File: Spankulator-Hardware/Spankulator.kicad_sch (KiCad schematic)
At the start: 106 parts, among them J1 3.5mm Jack, J12 Arduino Socket, J13 Arduino Socket, J2 2x5 Header, J3 3.5mm Jack, J4 3.5mm Jack, J5 3.5mm Jack, J6 3.5mm Jack, J7 2x5 Header, J9 Display Header, Q1 2N3904, Q2 VP2106/ZVP3306A, Q3 2N7000, Q4 VP2106/ZVP3306A, Q5 2N7000, Q7 2N7000, Q8 2N7000, SW1 Adj, SW2 Push Button, SW3 Push Button, SW4 Push Button, SW5 Push Button, SW6 Push Button, SW7 Push Button, SW8 Push Button, U1 TL072CP, U2 CD4013BE, U3 TL072CP, U4 MC78L05_TO92, U5 LP2950-3.3_TO92, U6 MAX7480, U7 MB85RC256

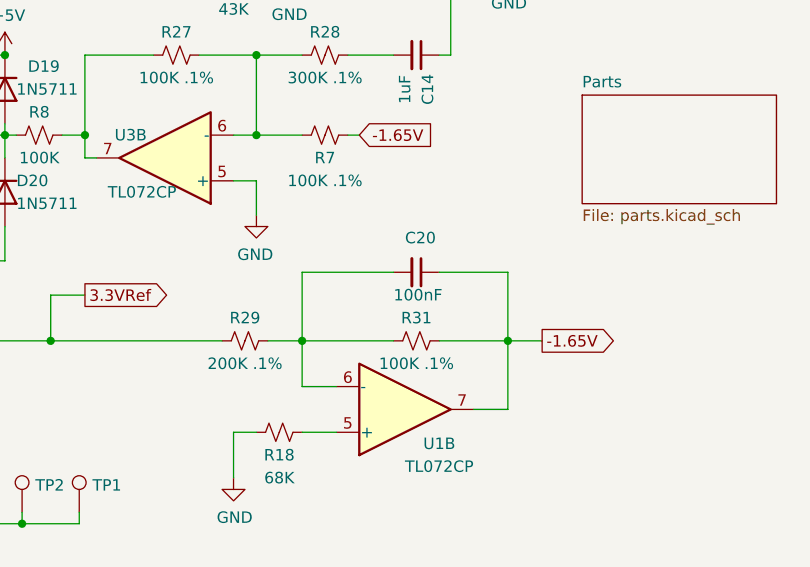
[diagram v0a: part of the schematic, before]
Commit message: Fixes parts too close
Fixes gain pot bumping into Exp connector.
Moves all TPs to board top
More components lay flat now
Adds Argh Ptoo face to silkscreen
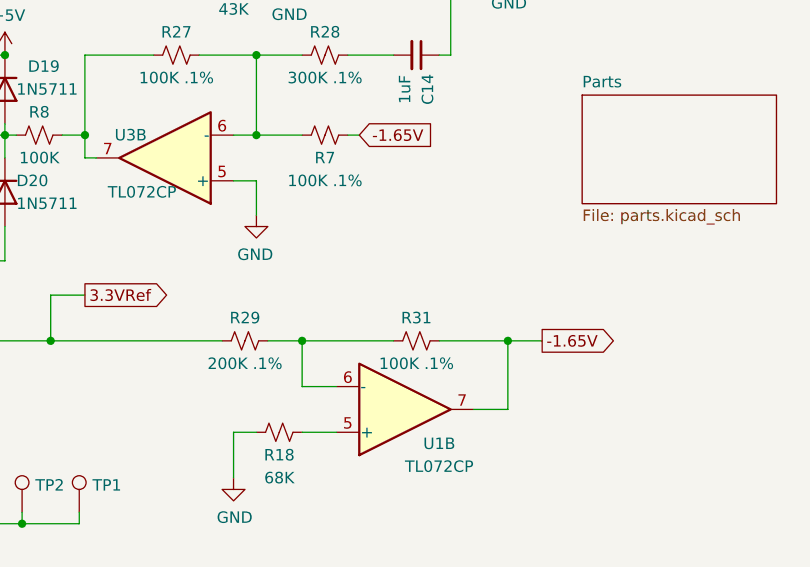
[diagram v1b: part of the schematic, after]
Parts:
- removed C20: 100nF, Capacitor_THT:C_Disc_D4.3mm_W1.9mm_P5.00mm, symbol Device:C_Small
- C16: LCSC Part # (none) -> C263193
- D8: footprint Diode_THT:D_DO-35_SOD27_P2.54mm_Vertical_AnodeUp -> Diode_THT:D_DO-35_SOD27_P7.62mm_Horizontal
- R16, R30, R31: footprint Resistor_THT:R_Axial_DIN0207_L6.3mm_D2.5mm_P2.54mm_Vertical -> Resistor_THT:R_Axial_DIN0207_L6.3mm_D2.5mm_P10.16mm_Horizontal
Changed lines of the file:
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@@
   (title_block
     (title "Spankulator")
-    (rev "5.1")
+    (rev "5.2")
     (company "Greenface Labs")
   )
@@
     (stroke (width 0) (type default) (color 0 0 0 0))
   )
-  (wire (pts (xy 247.65 128.27) (xy 247.65 135.89))
-    (stroke (width 0) (type default) (color 0 0 0 0))
-  )
   (wire (pts (xy 149.86 168.91) (xy 149.86 182.88))
     (stroke (width 0) (type default) (color 0 0 0 0))
@@
     (stroke (width 0) (type default) (color 0 0 0 0))
   )
-  (wire (pts (xy 224.79 128.27) (xy 224.79 135.89))
-    (stroke (width 0) (type default) (color 0 0 0 0))
-  )
   (wire (pts (xy 74.93 91.44) (xy 71.12 91.44))
     (stroke (width 0) (type default) (color 0 0 0 0))
@@
     (stroke (width 0) (type default) (color 0 0 0 0))
   )
-  (wire (pts (xy 240.03 128.27) (xy 247.65 128.27))
-    (stroke (width 0) (type default) (color 0 0 0 0))
-  )
   (wire (pts (xy 160.02 128.27) (xy 160.02 125.73))
     (stroke (width 0) (type default) (color 0 0 0 0))
@@
     (stroke (width 0) (type default) (color 0 0 0 0))
   )
-  (wire (pts (xy 234.95 128.27) (xy 224.79 128.27))
-    (stroke (width 0) (type default) (color 0 0 0 0))
-  )
   (wire (pts (xy 69.85 60.96) (xy 101.6 60.96))
     (stroke (width 0) (type default) (color 0 0 0 0))
@@
     (property "Reference" "R31" (id 0) (at 237.49 133.35 90))
     (property "Value" "100K .1%" (id 1) (at 237.49 138.43 90))
-    (property "Footprint" "Resistor_THT:R_Axial_DIN0207_L6.3mm_D2.5mm_P2.54mm_Vertical" (id 2) (at 237.49 135.89 0)
+    (property "Footprint" "Resistor_THT:R_Axial_DIN0207_L6.3mm_D2.5mm_P10.16mm_Horizontal" (id 2) (at 237.49 135.89 0)
       (effects (font (size 1.27 1.27)) hide)
     )
@@
       (effects (font (size 1.27 1.27)) hide)
     )
+    (property "LCSC Part #" "C263193" (id 5) (at 160.02 123.19 0)
+      (effects (font (size 1.27 1.27)) hide)
+    )
     (pin "1")
     (pin "2")
@@
     (property "Reference" "R30" (id 0) (at 191.77 60.96 90))
     (property "Value" "95.3K 1%" (id 1) (at 191.77 66.04 90))
-    (property "Footprint" "Resistor_THT:R_Axial_DIN0207_L6.3mm_D2.5mm_P2.54mm_Vertical" (id 2) (at 191.77 63.5 0)
+    (property "Footprint" "Resistor_THT:R_Axial_DIN0207_L6.3mm_D2.5mm_P10.16mm_Horizontal" (id 2) (at 191.77 63.5 0)
       (effects (font (size 1.27 1.27)) hide)
     )
@@
     (property "Reference" "R16" (id 0) (at 201.93 17.78 0))
     (property "Value" "100K" (id 1) (at 201.93 20.32 0))
-    (property "Footprint" "Resistor_THT:R_Axial_DIN0207_L6.3mm_D2.5mm_P2.54mm_Vertical" (id 2) (at 198.12 19.05 0)
+    (property "Footprint" "Resistor_THT:R_Axial_DIN0207_L6.3mm_D2.5mm_P10.16mm_Horizontal" (id 2) (at 198.12 19.05 0)
       (effects (font (size 1.27 1.27)) hide)
     )
@@
     (pin "3")
   )
-  (symbol (lib_id "Device:C_Small") (at 237.49 128.27 270) (unit 1)
-    (in_bom yes) (on_board yes)
-    (property "Reference" "C20" (id 0) (at 236.22 124.46 90)
-      (effects (font (size 1.27 1.27)) (justify left))
-    )
-    (property "Value" "100nF" (id 1) (at 234.95 130.81 90)
-      (effects (font (size 1.27 1.27)) (justify left))
-    )
-    (property "Footprint" "Capacitor_THT:C_Disc_D4.3mm_W1.9mm_P5.00mm" (id 2) (at 237.49 128.27 0)
-      (effects (font (size 1.27 1.27)) hide)
-    )
-    (property "Datasheet" "http://datasheets.avx.com/SR-Series.pdf" (id 3) (at 237.49 128.27 0)
-      (effects (font (size 1.27 1.27)) hide)
-    )
-    (property "Digi-Key Part" "399-9877-1-ND" (id 4) (at 237.49 128.27 0)
-      (effects (font (size 1.27 1.27)) hide)
-    )
-    (property "LCSC Part #" "" (id 5) (at 237.49 128.27 0)
-      (effects (font (size 1.27 1.27)) hide)
-    )
-    (property "Build Type" "split" (id 6) (at 237.49 128.27 0)
-      (effects (font (size 1.27 1.27)) hide)
-    )
-    (pin "1")
-    (pin "2")
-  )
   (symbol (lib_id "power:+12V") (at 111.76 43.18 0) (unit 1)
     (in_bom yes) (on_board yes)
@@
       (effects (font (size 1.27 1.27)) (justify left))
     )
-    (property "Footprint" "Diode_THT:D_DO-35_SOD27_P2.54mm_Vertical_AnodeUp" (id 2) (at 146.685 184.785 0)
+    (property "Footprint" "Diode_THT:D_DO-35_SOD27_P7.62mm_Horizontal" (id 2) (at 146.685 184.785 0)
       (effects (font (size 1.27 1.27)) hide)
     )
@@
       (reference "C19") (unit 1) (value "10nF") (footprint "Capacitor_THT:C_Disc_D4.3mm_W1.9mm_P5.00mm")
     )
-    (path "/00000000-0000-0000-0000-0000620c5895"
-      (reference "C20") (unit 1) (value "100nF") (footprint "Capacitor_THT:C_Disc_D4.3mm_W1.9mm_P5.00mm")
-    )
     (path "/83a7ca09-b4fd-493e-8bbb-bd08be746ed9"
       (reference "C21") (unit 1) (value "100nF") (footprint "Capacitor_THT:C_Disc_D4.3mm_W1.9mm_P5.00mm")
@@
     )
     (path "/ffb6f1cc-502c-44ab-af5c-1e16fc95c761"
-      (reference "D8") (unit 1) (value "1N5711") (footprint "Diode_THT:D_DO-35_SOD27_P2.54mm_Vertical_AnodeUp")
+      (reference "D8") (unit 1) (value "1N5711") (footprint "Diode_THT:D_DO-35_SOD27_P7.62mm_Horizontal")
     )
     (path "/e4a3c8d3-a1ce-43f4-982e-7455d6f0fe81"
@@
       (reference "D20") (unit 1) (value "1N5711") (footprint "Diode_THT:D_DO-35_SOD27_P7.62mm_Horizontal")
     )
+    (path "/681cdba4-7e5c-45e3-bb80-441c833d63d5/f2eba3d0-6b09-4a9e-bb1e-84fba106eb8c"
+      (reference "GR1") (unit 1) (value "small_logo") (footprint "panel:small_face")
+    )
     (path "/681cdba4-7e5c-45e3-bb80-441c833d63d5/312fd6ac-da80-4a7f-a4f9-8dafa09dc33f"
       (reference "H1") (unit 1) (value "MountingHole") (footprint "MountingHole:MountingHole_2.5mm")
@@
     )
     (path "/00000000-0000-0000-0000-000061094a97"
-      (reference "R16") (unit 1) (value "100K") (footprint "Resistor_THT:R_Axial_DIN0207_L6.3mm_D2.5mm_P2.54mm_Vertical")
+      (reference "R16") (unit 1) (value "100K") (footprint "Resistor_THT:R_Axial_DIN0207_L6.3mm_D2.5mm_P10.16mm_Horizontal")
     )
     (path "/00000000-0000-0000-0000-00005f427c66"
@@
     )
     (path "/00000000-0000-0000-0000-000060a0db56"
-      (reference "R30") (unit 1) (value "95.3K 1%") (footprint "Resistor_THT:R_Axial_DIN0207_L6.3mm_D2.5mm_P2.54mm_Vertical")
+      (reference "R30") (unit 1) (value "95.3K 1%") (footprint "Resistor_THT:R_Axial_DIN0207_L6.3mm_D2.5mm_P10.16mm_Horizontal")
     )
     (path "/00000000-0000-0000-0000-00006053a1ea"
-      (reference "R31") (unit 1) (value "100K .1%") (footprint "Resistor_THT:R_Axial_DIN0207_L6.3mm_D2.5mm_P2.54mm_Vertical")
+      (reference "R31") (unit 1) (value "100K .1%") (footprint "Resistor_THT:R_Axial_DIN0207_L6.3mm_D2.5mm_P10.16mm_Horizontal")
     )
     (path "/00000000-0000-0000-0000-00005fd12529"

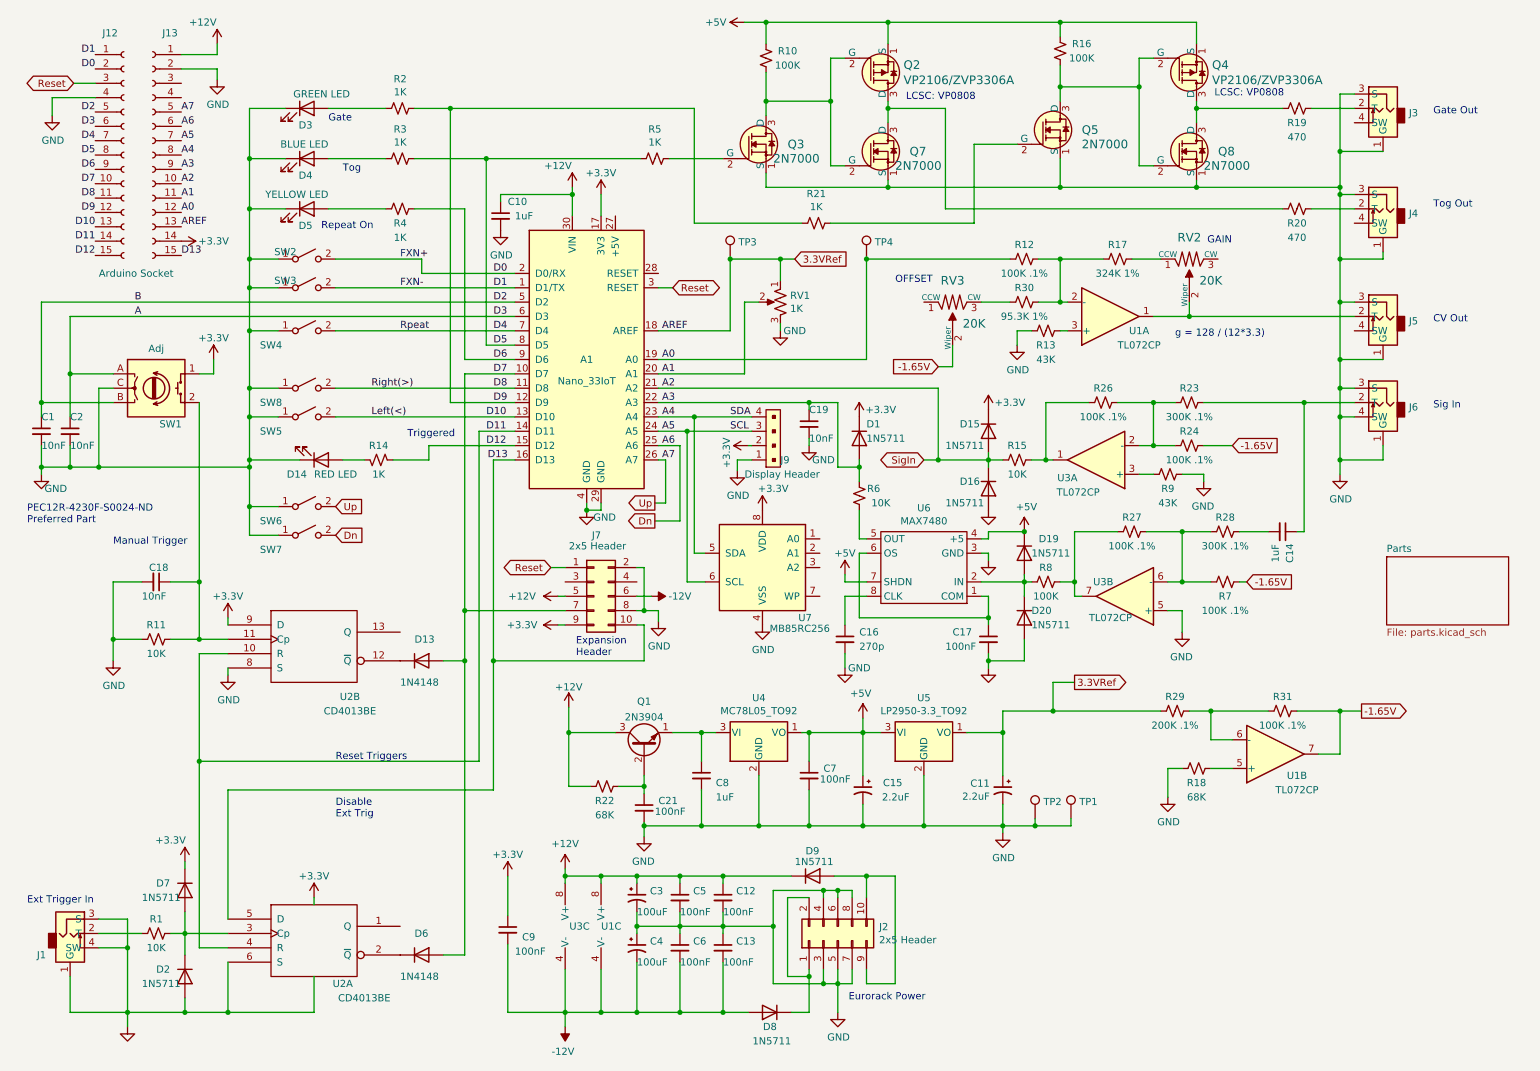
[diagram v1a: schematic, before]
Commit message: Replaces FET outputs with OP Amp.
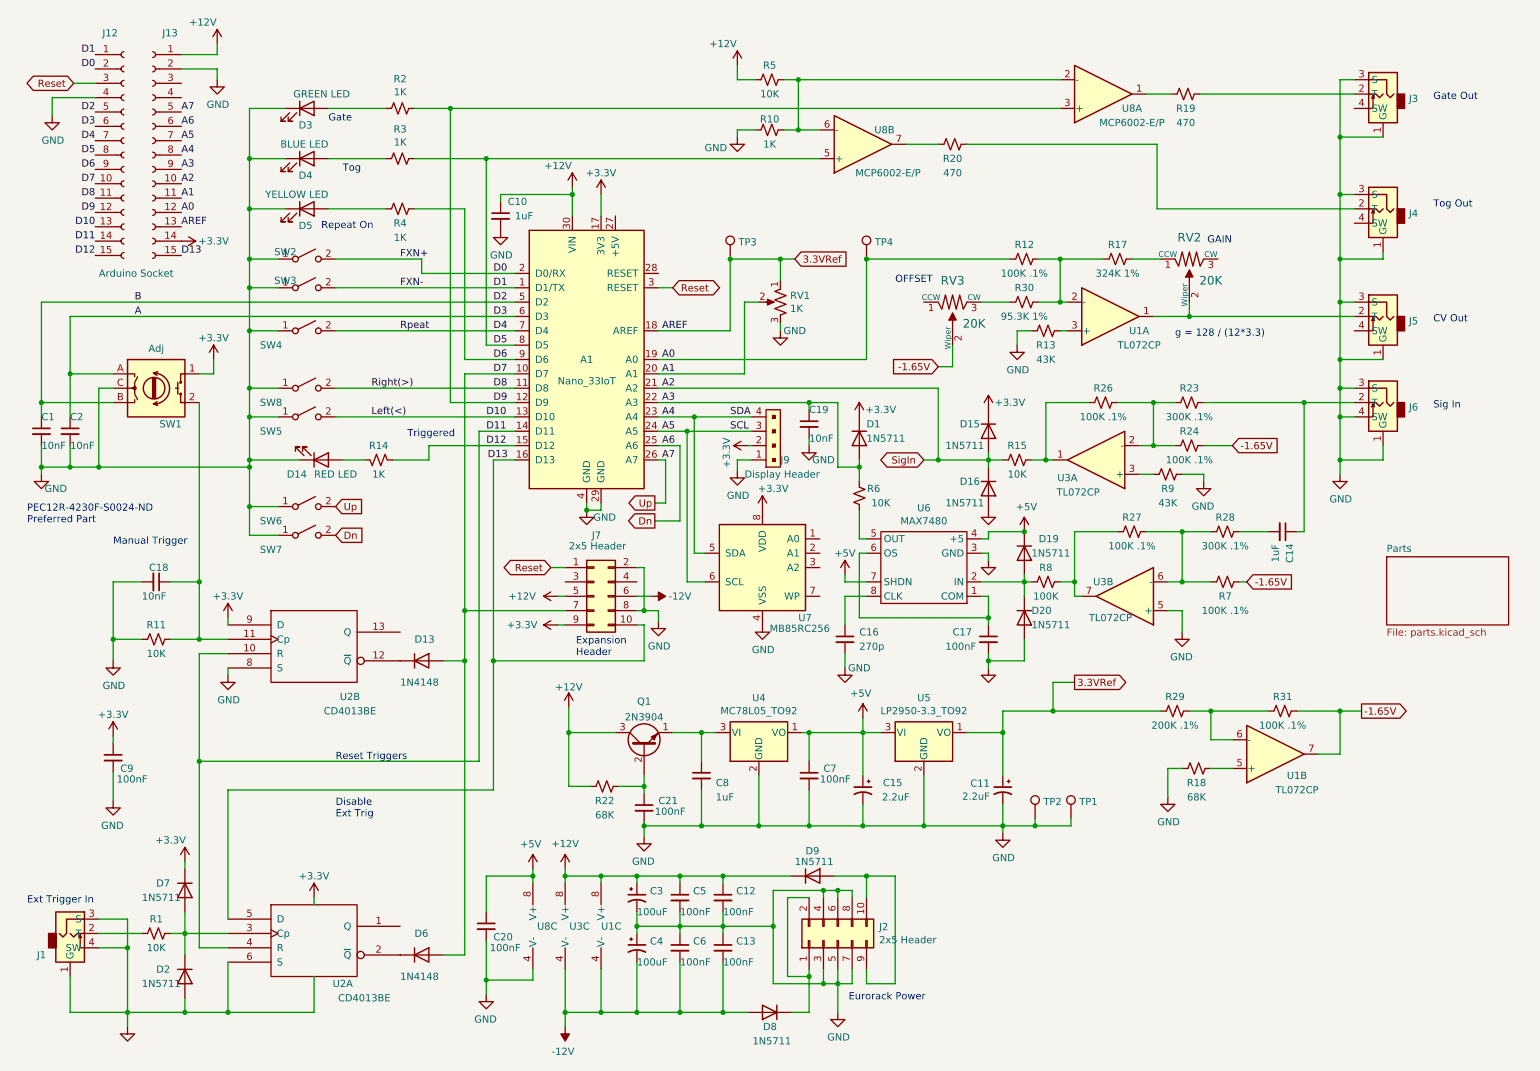
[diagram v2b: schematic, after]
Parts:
- removed Q2, Q4: VP2106/ZVP3306A, digikey-footprints:TO-92-3_Formed_Leads, symbol greenface-symbols:VP2106
- removed Q3, Q5, Q7, Q8: 2N7000, digikey-footprints:TO-92-3_Formed_Leads, symbol dk_Transistors-FETs-MOSFETs-Single:2N7000
- removed R16: 100K, Resistor_THT:R_Axial_DIN0207_L6.3mm_D2.5mm_P10.16mm_Horizontal, symbol Device:R_Small_US
- removed R21: 1K, Resistor_THT:R_Axial_DIN0207_L6.3mm_D2.5mm_P10.16mm_Horizontal, symbol Device:R_Small_US
- added C20: 100nF, Capacitor_THT:C_Disc_D4.3mm_W1.9mm_P5.00mm, symbol Device:C_Small
- added U8: MCP6002-E/P, Package_DIP:DIP-8_W7.62mm_Socket, symbol Amplifier_Operational:TL072
- C1, C18, C19, C2: LCSC Part # C162686 -> C263180
- R10: value 100K -> 1K; Digi-Key Part 2019-CF1/4CT52R104JCT-ND -> CF14JT1K00CT-ND; LCSC Part # C120103 -> C66649
- R5: value 1K -> 10K; Digi-Key Part CF14JT1K00CT-ND -> CF14JT10K0CT-ND; LCSC Part # C66649 -> C433778
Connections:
- net +12V: now also R5.2
- net +5V: now also C20.1, U8.8 (V+); no longer R10.1
- net -12V: no longer C9.2
- net D5: now also U8.5 (+); no longer R5.2
- net D9: now also U8.3 (+)
- net GND: now also C9.2, R10.2, C20.2, U8.4 (V-)
- net at R19.1: now also U8.1
- net at R20.1: now also U8.7
- net at R5.1: now also R10.1, U8.2 (-), U8.6 (-)
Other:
- note removed: "LCSC: VP0808"
- moved on the sheet: C9, J3, R19, R20
